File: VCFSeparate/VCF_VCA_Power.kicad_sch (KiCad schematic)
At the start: 4 parts, among them J1 A_Power, U1 LM13700, U2 LM13700, U3 LM13700

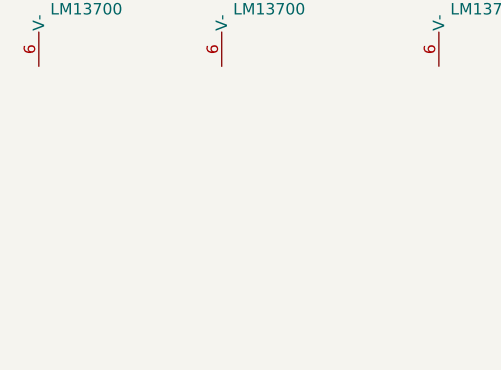
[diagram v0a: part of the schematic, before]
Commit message: VCFSeparate
レゾナンスVCAを追加
コントローラー系を作成中
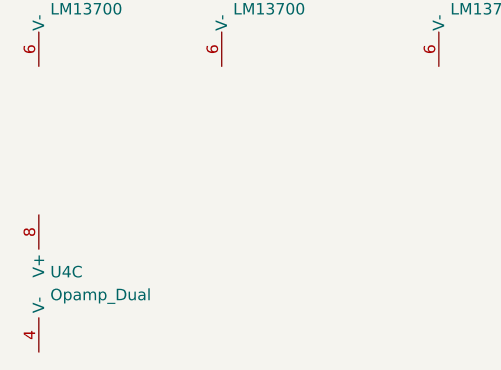
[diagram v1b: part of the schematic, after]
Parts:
- added U4: Opamp_Dual, Package_DIP:DIP-8_W7.62mm_LongPads, symbol Device:Opamp_Dual
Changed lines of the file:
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@@
+	)
+	(symbol
+		(lib_id "Device:Opamp_Dual")
+		(at 41.91 68.58 0)
+		(unit 3)
+		(exclude_from_sim no)
+		(in_bom yes)
+		(on_board yes)
+		(dnp no)
+		(fields_autoplaced yes)
+		(property "Reference" "U4"
+			(at 40.64 67.3099 0)
+			(effects
+				(font
+					(size 1.27 1.27)
+				)
+				(justify left)
+			)
+		)
+		(property "Value" "Opamp_Dual"
+			(at 40.64 69.8499 0)
+			(effects
+				(font
+					(size 1.27 1.27)
+				)
+				(justify left)
+			)
+		)
+		(property "Footprint" "Package_DIP:DIP-8_W7.62mm_LongPads"
+			(at 41.91 68.58 0)
+			(effects
+				(font
+					(size 1.27 1.27)
+				)
+				(hide yes)
+			)
+		)
+		(property "Datasheet" "~"
+			(at 41.91 68.58 0)
+			(effects
+				(font
+					(size 1.27 1.27)
+				)
+				(hide yes)
+			)
+		)
+		(property "Description" "Dual operational amplifier"
+			(at 41.91 68.58 0)
+			(effects
+				(font
+					(size 1.27 1.27)
+				)
+				(hide yes)
+			)
+		)
+		(property "Sim.Library" "${KICAD7_SYMBOL_DIR}/Simulation_SPICE.sp"
+			(at 41.91 68.58 0)
+			(effects
+				(font
+					(size 1.27 1.27)
+				)
+				(hide yes)
+			)
+		)
+		(property "Sim.Name" "kicad_builtin_opamp_dual"
+			(at 41.91 68.58 0)
+			(effects
+				(font
+					(size 1.27 1.27)
+				)
+				(hide yes)
+			)
+		)
+		(property "Sim.Device" "SUBCKT"
+			(at 41.91 68.58 0)
+			(effects
+				(font
+					(size 1.27 1.27)
+				)
+				(hide yes)
+			)
+		)
+		(property "Sim.Pins" "1=out1 2=in1- 3=in1+ 4=vee 5=in2+ 6=in2- 7=out2 8=vcc"
+			(at 41.91 68.58 0)
+			(effects
+				(font
+					(size 1.27 1.27)
+				)
+				(hide yes)
+			)
+		)
+		(pin "3"
+		)
+		(pin "1"
+		)
+		(pin "2"
+		)
+		(pin "6"
+		)
+		(pin "5"
+		)
+		(pin "4"
+		)
+		(pin "7"
+		)
+		(pin "8"
+		)
+		(instances
+			(project "VCFSeparate"
+				(path "/02fc5d1f-a2a3-4ec9-a454-0bdd0b1ddad0/313889bb-bff5-4b3e-ac2c-df6eddbb7736"
+					(reference "U4")
+					(unit 3)
+				)
+			)
+		)
 	)
 	(symbol

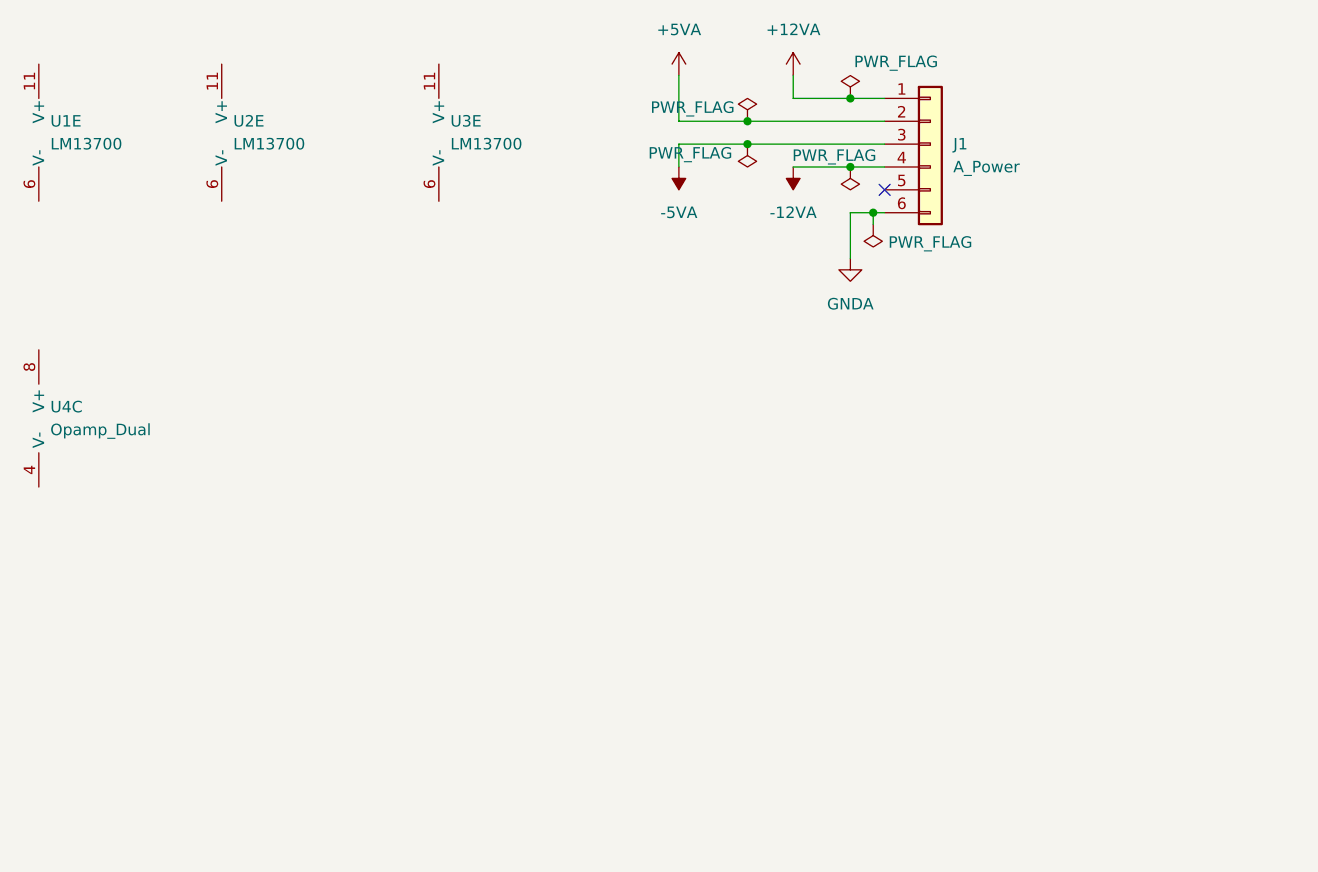
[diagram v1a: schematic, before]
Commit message: MC2
VCO,VCF+VCA,Powerを登録
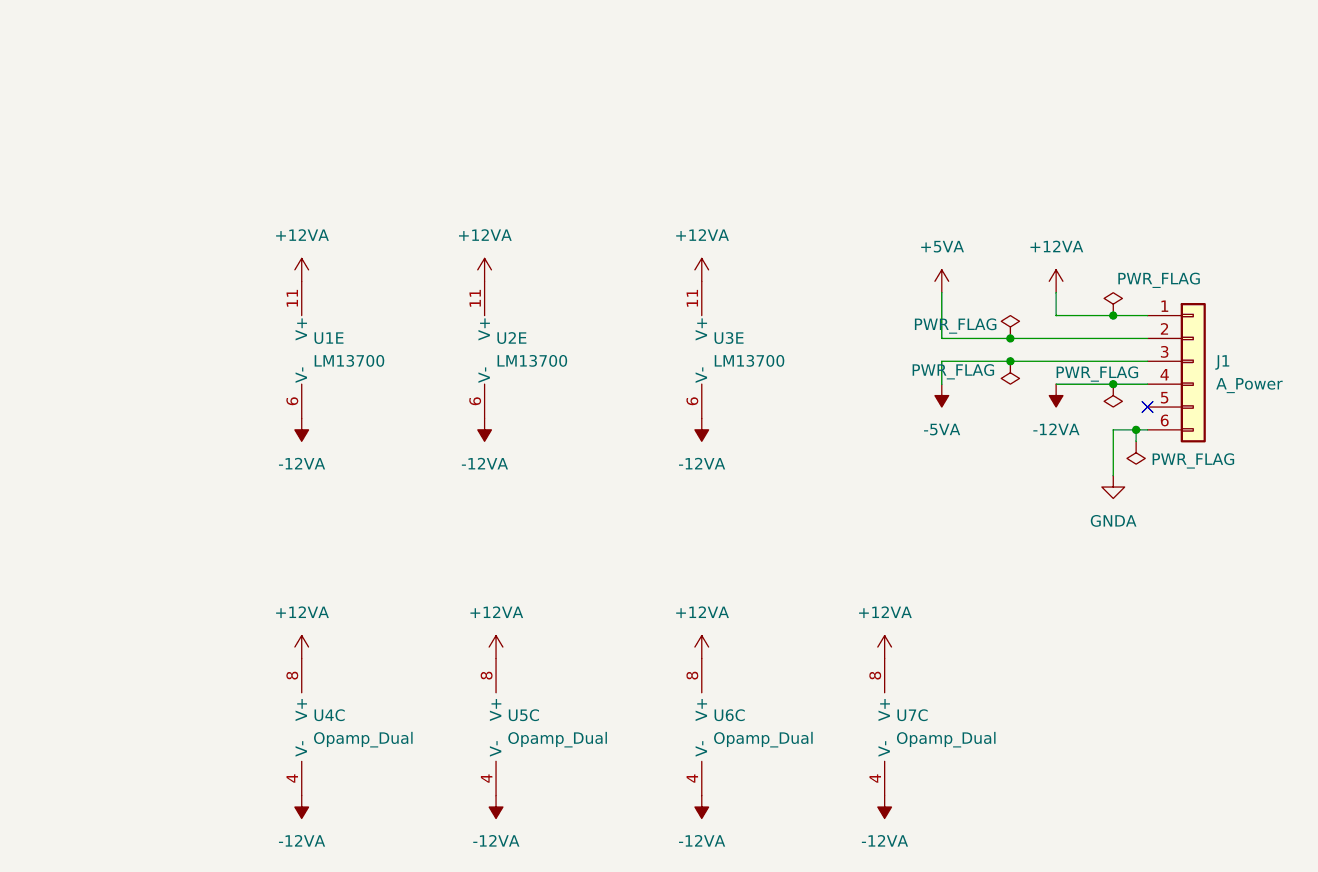
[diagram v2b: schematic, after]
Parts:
- added U5, U6, U7: Opamp_Dual, Package_SO:SO-8_3.9x4.9mm_P1.27mm, symbol Device:Opamp_Dual
- U4: footprint Package_DIP:DIP-8_W7.62mm_LongPads -> Package_SO:SO-8_3.9x4.9mm_P1.27mm
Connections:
- net +12VA: now also U1.11 (V+), U2.11 (V+), U3.11 (V+), U4.8 (V+), U5.8 (V+), U6.8 (V+), U7.8 (V+)
- net -12VA: now also U1.6 (V-), U2.6 (V-), U3.6 (V-), U4.4 (V-), U5.4 (V-), U6.4 (V-), U7.4 (V-)
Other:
- moved on the sheet: J1, U1E, U2E, U3E
